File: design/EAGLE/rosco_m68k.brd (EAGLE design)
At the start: 160 x 100 mm, 74 parts, among them IC1 74LS04N, IC10 74LS32N, IC11 NE555N, IC12 74LS01N, IC2 MC68010P10, IC3 ATF16V8QL-15PU, IC4 74LS93N, IC5 74S20N, IC6 MC68901P, IC7 74LS08N, IC8 74LS08N, IC9 74LS174N, Q1 1.8432MHz, Q2 8MHz, U1 AT28C64B-15PU, U2 AT28C64B-15PU, U3 AS6C4008-55PCN, U4 AS6C4008-55PCN

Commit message: New PCB design
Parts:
- removed C29: 100nF, capacitor-wima:C2.5-3
- removed C30: 100uF, rcl:E2,5-5
- removed C31: 400uF, rcl:E3,5-10
- removed IC10: 74LS32N, 74xx-eu:DIL14
- removed IC11: NE555N, linear:DIL08
- removed IC12: 74LS01N, 74xx-eu:DIL14
- removed R18: 4K7, rcl:0207/10
- added JP3: (no value), pinhead:2X30
- added JP4: (no value), pinhead:2X02
- added U$1: (no value), oshw:OSHW_8MM
- C10: value 100nF -> 33pF
- C12: value 33pF -> 100nF
- C16, C2, C25, C27, C4: value 100nF -> 100uF; device capacitor-wima:C2.5-3 -> rcl:E2,5-5
- C19, C3, C5: value 100uF -> 100nF; device rcl:E2,5-5 -> capacitor-wima:C2.5-3
- C20, C22: value 100nF -> 22pF
- C24, C26: value 22pF -> 100nF
- C28: value 100uF -> 400uF; device rcl:E2,5-5 -> rcl:E3,5-10
- IC1: value 74LS04N -> MC68010P10; device 74xx-eu:DIL14 -> micro-mc68000:DIL64
- IC2: value MC68010P10 -> ATF16V8QL-15PU; device micro-mc68000:DIL64 -> atmel:DIL20
- IC3: value ATF16V8QL-15PU -> 74LS93N; device atmel:DIL20 -> 74xx-eu:DIL14
- IC4: value 74LS93N -> MC68901P; device 74xx-eu:DIL14 -> micro-mc68000:DIL48
- IC5: value 74S20N -> ATF16V8QL-15PU; device 74xx-eu:DIL14 -> atmel:DIL20
- IC6: value MC68901P -> 74LS174N; device micro-mc68000:DIL48 -> 74xx-eu:DIL16
- IC7: value 74LS08N -> 74LS04N
- IC8: value 74LS08N -> NE555N; device 74xx-eu:DIL14 -> linear:DIL08
- IC9: value 74LS174N -> 74LS01N; device 74xx-eu:DIL16 -> 74xx-eu:DIL14
- JP1: device pinhead:1X03 -> pinhead:1X04
- R10, R5: value 4K7 -> 1K2
- R11, R6: value 1K2 -> 4K7
- R12: value 4K7 -> 2K2
- R13: value 2K2 -> 270R
- R14: value 270R -> 330R
- R16: value 330R -> 4K7
- moved JP2 152.4 mm to (156.2, 5.08), turned to 270 degrees
- moved C26 148.8 mm to (156.2, 62.2), turned to 0 degrees
- moved C24 144.2 mm to (151.1, 62.2), turned to 0 degrees
- moved C25 141.5 mm to (153.7, 41.3)
- moved IC8 135.0 mm to (153.4, 52.1)
- moved C13 115.3 mm to (135.3, 72.4)
- moved IC4 112.0 mm to (131.4, 35.6)
- moved R13 110.2 mm to (156.8, 82.5), turned to 90 degrees
- moved C5 108.0 mm to (41.9, 3.81)
- moved C27 101.3 mm to (147.0, 17.8)
- moved R14 98.8 mm to (147.3, 80.0), turned to 90 degrees
- moved C28 98.8 mm to (147.3, 5.71), turned to 270 degrees
- moved C1 98.3 mm to (102.9, 87.9), turned to 90 degrees
- moved LED3 94.6 mm to (144.8, 92.1)
- moved C14 94.4 mm to (127.0, 72.4)
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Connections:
- removed net IACK: IC1.10, IC10.5
- removed net N$11: IC6.10, IC6.16, IC6.7
- removed net N$12: IC6.22, LED1.K
- removed net N$13: IC6.9, JP1.1
- removed net N$14: IC6.8, JP1.2
- removed net N$15: IC8.6, IC8.9
- removed net N$17: IC6.23, LED2.K
- removed net N$18: IC6.29, JP1.3
- removed net N$2: IC2.21, R1.1
- removed net N$24: IC8.10, IC8.3
- removed net N$25: IC10.4, IC8.8
- removed net N$27: IC10.1, IC8.11
- removed net N$28: IC10.6, IC7.4
- removed net N$29: IC10.3, IC7.5
- removed net N$7: C11.1, IC6.17, Q1.1
- removed net N$8: C12.1, IC6.18, Q1.2
- new net MFPIO0: IC4.22, LED1.K
- new net MFPIO1: IC4.23, LED2.K
- new net MFPXTAL1: C10.1, IC4.17, Q1.1
- new net MFPXTAL2: C11.1, IC4.18, Q1.2
- new net UARTCLK: IC4.10, IC4.16, IC4.7
- new net UARTCTS: IC4.29, JP1.4
- new net UARTRX: IC4.9, JP1.3
- new net UARTTX: IC4.8, JP1.2
- new net VPA: IC1.21, R1.1
- net /BOOT: now also IC2.9, IC6.15; no longer IC3.9, IC9.15
- net /HALT: now also IC1.17, IC9.1, IC9.8, IC9.9, R16.1; no longer IC12.1, IC12.8, IC12.9, IC2.17, R17.1
- net /IACK: now also IC2.18, IC4.45, IC5.13; no longer IC1.11, IC3.18, IC5.6, IC6.45, IC7.2, IC8.12
- net /IODTACK: now also IC4.46, IC5.9; no longer IC10.2, IC6.46, R4.1
- net /MFPDS: now also IC4.47, IC5.15; no longer IC6.47, IC7.3
- net /RAMOE: now also IC5.16; no longer IC1.2
- net A1: now also IC1.29, IC4.6, JP3.1; no longer IC2.29, IC6.6
- net A10: now also IC1.38, JP3.19; no longer IC2.38
- net A11: now also IC1.39, JP3.21; no longer IC2.39
- net A12: now also IC1.40, JP3.23; no longer IC2.40
- net A13: now also IC1.41, JP3.25; no longer IC2.41
- net A14: now also IC1.42, JP3.27; no longer IC2.42
- net A15: now also IC1.43, JP3.29; no longer IC2.43
- net A16: now also IC1.44, JP3.31; no longer IC2.44
- net A17: now also IC1.45, JP3.33; no longer IC2.45
- net A18: now also IC1.46, IC2.1, JP3.35; no longer IC2.46, IC3.1
- net A19: now also IC1.47, IC2.2, JP3.37; no longer IC2.47, IC3.2
- net A2: now also IC1.30, IC4.5, JP3.3; no longer IC2.30, IC6.5
- net A20: now also IC1.48, IC2.3, JP3.39; no longer IC2.48, IC3.3
- net A21: now also IC1.50, IC2.4, JP3.41; no longer IC2.50, IC3.4
- net A22: now also IC1.51, IC2.5, JP3.43; no longer IC2.51, IC3.5
- net A23: now also IC1.52, IC2.6, JP3.45; no longer IC2.52, IC3.6
- net A3: now also IC1.31, IC4.4, JP3.5; no longer IC2.31, IC6.4
- net A4: now also IC1.32, IC4.3, JP3.7; no longer IC2.32, IC6.3
- net A5: now also IC1.33, IC4.2, JP3.9; no longer IC2.33, IC6.2
- net A6: now also IC1.34, JP3.11; no longer IC2.34
- net A7: now also IC1.35, JP3.13; no longer IC2.35
- net A8: now also IC1.36, JP3.15; no longer IC2.36
- net A9: now also IC1.37, JP3.17; no longer IC2.37
- net AS: now also IC1.6, IC2.11, IC6.9, JP3.47; no longer IC2.6, IC3.11, IC9.9
- net BERR: now also IC1.22, JP3.49, R11.1; no longer IC2.22, R12.1
- net BG: now also IC1.11, JP3.51; no longer IC2.11
- net BGACK: now also IC1.12, JP3.53, R9.1; no longer IC2.12, R10.1
- net BR: now also IC1.13, JP3.55, R8.1; no longer IC2.13, R9.1
- net CLK: now also IC1.15, IC3.14, IC7.6, JP3.4; no longer IC1.8, IC2.15, IC4.14
- net D0: now also IC1.5, IC4.37, JP4.1; no longer IC2.5, IC6.37
- net D1: now also IC1.4, IC4.38, JP4.3; no longer IC2.4, IC6.38
- net D10: now also IC1.59, JP3.48; no longer IC2.59
- net D11: now also IC1.58, JP3.46; no longer IC2.58
- net D12: now also IC1.57, JP3.44; no longer IC2.57
- net D13: now also IC1.56, JP3.42; no longer IC2.56
- net D14: now also IC1.55, JP3.40; no longer IC2.55
- net D15: now also IC1.54, JP3.38; no longer IC2.54
- net D2: now also IC1.3, IC4.39, JP4.4; no longer IC2.3, IC6.39
- net D3: now also IC1.2, IC4.40, JP4.2; no longer IC2.2, IC6.40
- net D4: now also IC1.1, IC4.41, JP3.60; no longer IC2.1, IC6.41
- net D5: now also IC1.64, IC4.42, JP3.58; no longer IC2.64, IC6.42
- net D6: now also IC1.63, IC4.43, JP3.56; no longer IC2.63, IC6.43
- net D7: now also IC1.62, IC4.44, JP3.54; no longer IC2.62, IC6.44
- net D8: now also IC1.61, JP3.52; no longer IC2.61
- net D9: now also IC1.60, JP3.50; no longer IC2.60
- net DTACK: now also IC1.10, IC5.14, JP3.57; no longer IC2.10, IC7.6
- net EVENRAMSEL: now also IC2.12, IC5.7, JP3.8; no longer IC3.12, IC8.2
- net EVENROMSEL: now also IC2.14, IC5.6, JP3.10; no longer IC3.14, IC8.5
- net EXPSEL: now also IC2.17, JP3.18; no longer IC3.17
- net FC0: now also IC1.28, IC5.1, JP3.20; no longer IC2.28, IC5.5
- net FC1: now also IC1.27, IC5.2, JP3.22; no longer IC2.27, IC5.4
- net FC2: now also IC1.26, IC5.3, JP3.24; no longer IC2.26, IC5.1, IC5.2
- net GND: now also C16.-, C19.2, C2.-, C25.-, C27.-, C3.2, C4.-, C5.2, IC1.16, IC1.53, IC2.10, IC3.1, IC3.2, IC3.3, IC4.19, IC4.20, IC4.34, IC4.36, IC5.11, IC6.13, IC6.4, IC6.8, IC7.11, IC8.1, IC9.11, IC9.12, IC9.7, JP1.1, JP3.6, R13.1; no longer C16.2, C19.-, C2.2, C21.2, C26.2, C27.2, C3.-, C30.-, C31.-, C4.2, C5.-, IC1.13, IC1.7, IC10.10, IC10.12, IC10.13, IC10.7, IC10.9, IC11.1, IC12.11, IC12.12, IC12.7, IC2.16, IC2.53, IC4.1, IC4.10, IC4.2, IC4.3, IC5.12, IC5.13, IC5.7, IC5.9, IC6.19, IC6.20, IC6.34, IC6.36, IC7.10, IC7.12, IC8.7, IC9.13, IC9.4, IC9.8, R15.1
- net IOSEL: now also IC2.16, IC4.48, IC5.8, JP3.16; no longer IC3.16, IC6.48, IC8.13
- net IPL0: now also IC1.25, JP3.26, R7.1; no longer IC2.25, R8.1
- net IPL1: now also IC1.24, JP3.28, R6.1; no longer IC2.24, R7.1
- net IPL2: now also IC1.23, IC4.32, JP3.30, R4.1; no longer IC2.23, IC6.32, R5.1
- net LDS: now also IC1.8, IC5.18, JP3.32; no longer IC3.8, IC7.1
- net MFPCLK: now also IC3.12, IC4.35; no longer IC4.12, IC6.35
- net N$16: now also IC6.11, IC6.7; no longer IC9.11, IC9.7
- net N$19: now also C26.2, IC8.5; no longer C29.2, IC11.5
- net N$20: now also R14.2; no longer R15.2
- net N$22: now also IC6.10, IC6.14; no longer IC9.10, IC9.14
- net N$23: now also IC6.2, IC6.6; no longer IC9.2, IC9.6
- net N$3: now also C21.1, IC7.2, R5.2; no longer C25.1, IC1.4, R6.2
- net N$33: now also IC9.10; no longer IC12.10
- net N$34: now also R15.1; no longer R16.1
- net N$35: now also IC8.3, IC9.2, IC9.3, IC9.5, IC9.6; no longer IC11.3, IC12.2, IC12.3, IC12.5, IC12.6
- net N$36: now also R13.2; no longer R14.2
- net N$37: now also C25.+, IC8.2, IC8.6, R12.1; no longer C28.+, IC11.2, IC11.6, R13.1
- net N$4: now also C21.2, IC7.3, R10.1; no longer C25.2, IC1.5, R11.1
- net N$5: now also C22.1, IC7.4, IC7.5, R10.2; no longer C26.1, IC1.6, IC1.9, R11.2
- net N$6: now also C20.1, IC7.1, R5.1; no longer C24.1, IC1.3, R6.1
- net ODDRAMSEL: now also IC2.13, IC5.5, JP3.12; no longer IC3.13, IC8.1
- net ODDROMSEL: now also IC2.15, IC5.4, JP3.14; no longer IC3.15, IC8.4
- net R/W: now also IC1.9, IC4.1, IC5.17, JP3.59; no longer IC1.1, IC2.9, IC6.1
- net RESET: now also IC1.18, IC4.21, IC6.1, IC9.4, JP3.36, R17.1; no longer IC12.4, IC2.18, IC6.21, IC9.1, R18.1
- net UDS: now also IC1.7, JP3.34; no longer IC3.7
- net VCC: now also C12.1, C16.+, C19.1, C2.+, C24.1, C26.1, C27.+, C28.+, C3.1, C4.+, C5.1, IC1.49, IC2.20, IC3.5, IC4.11, IC5.20, IC6.16, IC6.3, IC8.4, IC8.8, IC9.14, JP3.2, R11.2, R15.2, R6.2; no longer C10.1, C16.1, C19.+, C2.1, C20.1, C21.1, C22.1, C27.1, C29.1, C3.+, C30.+, C31.+, C4.1, C5.+, IC10.14, IC11.4, IC11.8, IC12.14, IC2.14, IC2.49, IC3.20, IC4.5, IC5.14, IC6.11, IC8.14, IC9.16, IC9.3, R10.2, R13.2, R18.2, R5.2
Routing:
- net GND: track 867.3 -> 0.00 mm, vias 2 -> 0
- net VCC: track 731.0 -> 0.00 mm, vias 3 -> 0
- net UARTTX: track 0.00 -> 165.9 mm, vias 0 -> 1
- net UARTRX: track 0.00 -> 159.3 mm, vias 0 -> 1
- net UARTCTS: track 0.00 -> 141.6 mm
- net A14: track 91.7 -> 217.3 mm, vias 0 -> 2
- net A11: track 154.2 -> 270.6 mm, vias 1 -> 0
- net N$17: track 109.6 -> 0.00 mm
- net N$12: track 108.0 -> 0.00 mm, vias 1 -> 0
- net A16: track 92.4 -> 197.6 mm, vias 0 -> 2
- net D1: track 172.9 -> 268.1 mm
- net A12: track 136.0 -> 226.4 mm, vias 1 -> 3
- net BERR: track 17.6 -> 106.1 mm, vias 1 -> 2
- net A10: track 132.0 -> 220.0 mm
- net EXPSEL: track 0.00 -> 86.4 mm
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- added copper zone on layer 2, net GND
- added copper zone on layer 15, net VCC
- removed copper zone on layer 16, net GND
- removed copper zone on layer 1, net VCC
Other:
- board text added: "1"
- board text added: "64"
- board text added: "EXPANSION - SEE http://github.com/roscopeco/rosco_m68k"
- board text added: "GND 5VDC"
- board text added: "GND TXD RXD CTS"
- board text added: "I0"
- board text added: "I1"
- board text added: "RUN RESET"
- board text added: "copyright 2019"
- board text added: "revision 0 (prototype)"
- board text added: "rosco_m68k revision zero"
- board text removed: "(c)2019"
- board text removed: "+5VDC"
- board text removed: "CLOCKS"
- board text removed: "EVEN RAM"
- board text removed: "EVEN ROM"
- board text removed: "GND"
- board text removed: "IO0"
- board text removed: "IO1"
- board text removed: "ODD RAM"
- board text removed: "ODD ROM"
- board text removed: "RESET"
- board text removed: "RUN"
- board text removed: "RXD TXD CTS"
- board text removed: "Version 1r0 (Prototype)"
- board text removed: "http://github.com/roscopeco/rosco_m68k"

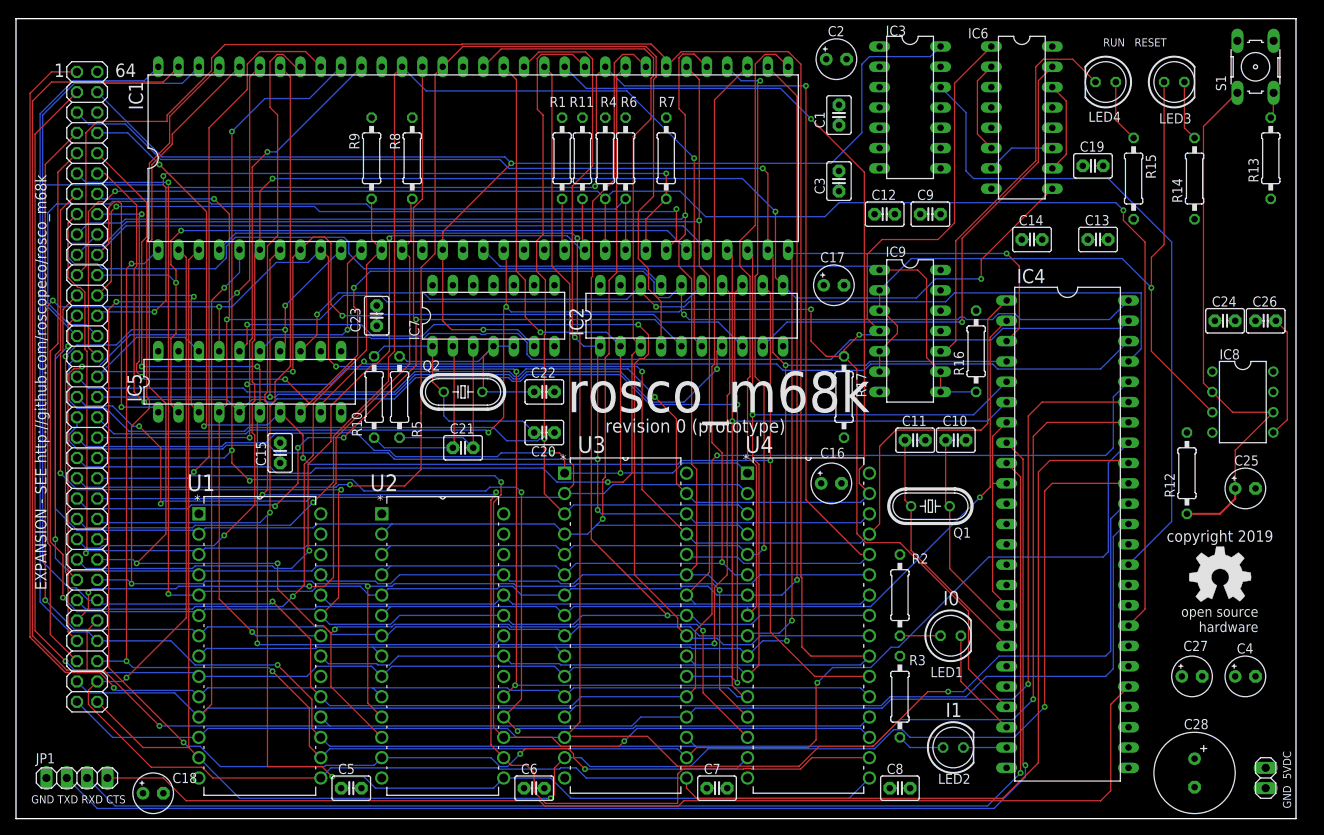
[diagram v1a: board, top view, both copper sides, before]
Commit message: Fix misplaced capacitor
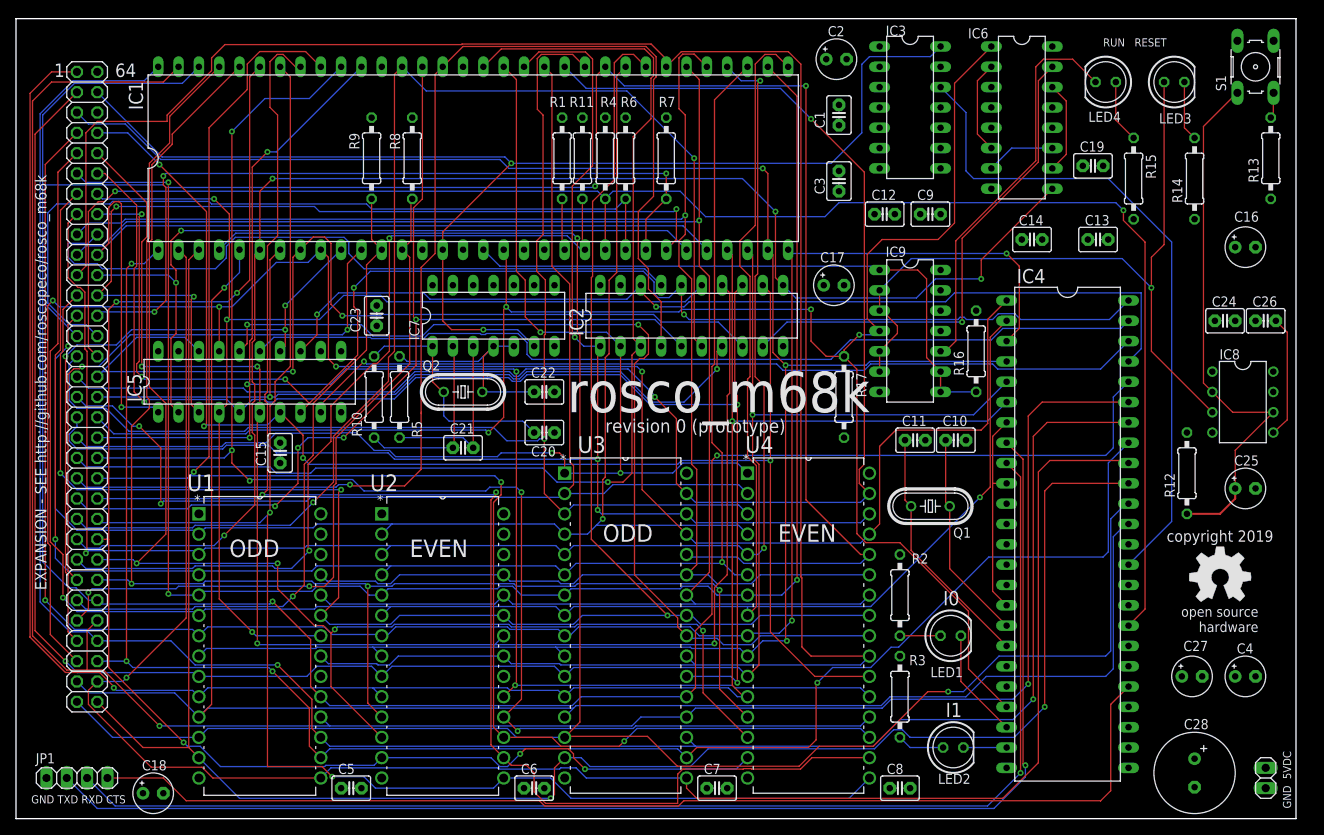
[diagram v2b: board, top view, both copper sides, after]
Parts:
- moved C16 59.6 mm to (153.7, 71.4)
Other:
- board text added: "EVEN"
- board text added: "ODD"
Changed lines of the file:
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@@
 <drawing>
 <settings>
-<setting alwaysvectorfont="yes"/>
+<setting alwaysvectorfont="no"/>
 <setting verticaltext="up"/>
 </settings>
@@
 <text x="157.48" y="26.9875" size="1.4224" layer="26" font="vector" rot="MR0">copyright 2019</text>
 <text x="143.8275" y="34.6075" size="1.4224" layer="25" font="vector">copyright 2019</text>
+<text x="26.67" y="32.7025" size="2.1844" layer="25">ODD</text>
+<text x="73.3425" y="34.6075" size="2.1844" layer="25">ODD</text>
+<text x="95.25" y="34.6075" size="2.1844" layer="25">EVEN</text>
+<text x="49.2125" y="32.7025" size="2.1844" layer="25">EVEN</text>
 </plain>
 <attributes>
@@
 <attribute name="VALUE" x="125.349" y="69.342" size="1.27" layer="27" ratio="10"/>
 </element>
-<element name="C16" library="rcl" library_urn="urn:adsk.eagle:library:334" package="E2,5-5" package3d_urn="urn:adsk.eagle:package:23344/1" value="100uF" x="101.9175" y="41.91" smashed="yes">
-<attribute name="NAME" x="100.5205" y="45.085" size="1.27" layer="25" ratio="10"/>
-<attribute name="POPULARITY" value="16" x="146.3675" y="-106.68" size="1.778" layer="27" display="off"/>
-<attribute name="SPICEPREFIX" value="C" x="146.3675" y="-106.68" size="1.778" layer="27" display="off"/>
-<attribute name="VALUE" x="99.568" y="37.592" size="1.27" layer="27" ratio="10"/>
+<element name="C16" library="rcl" library_urn="urn:adsk.eagle:library:334" package="E2,5-5" package3d_urn="urn:adsk.eagle:package:23344/1" value="100uF" x="153.67" y="71.4375" smashed="yes">
+<attribute name="NAME" x="152.273" y="74.6125" size="1.27" layer="25" ratio="10"/>
+<attribute name="POPULARITY" value="16" x="198.12" y="-77.1525" size="1.778" layer="27" display="off"/>
+<attribute name="SPICEPREFIX" value="C" x="198.12" y="-77.1525" size="1.778" layer="27" display="off"/>
+<attribute name="VALUE" x="151.3205" y="67.1195" size="1.27" layer="27" ratio="10"/>
 </element>
 <element name="C17" library="rcl" library_urn="urn:adsk.eagle:library:334" package="E2,5-5" package3d_urn="urn:adsk.eagle:package:23344/1" value="100uF" x="102.235" y="66.675" smashed="yes">
@@
 </element>
 <element name="C18" library="rcl" library_urn="urn:adsk.eagle:library:334" package="E2,5-5" package3d_urn="urn:adsk.eagle:package:23344/1" value="100uF" x="17.145" y="3.175" smashed="yes">
-<attribute name="NAME" x="19.558" y="4.445" size="1.27" layer="25" ratio="10"/>
+<attribute name="NAME" x="15.748" y="6.0325" size="1.27" layer="25" ratio="10"/>
 <attribute name="POPULARITY" value="16" x="84.455" y="-145.415" size="1.778" layer="27" display="off"/>
 <attribute name="SPICEPREFIX" value="C" x="84.455" y="-145.415" size="1.778" layer="27" display="off"/>
